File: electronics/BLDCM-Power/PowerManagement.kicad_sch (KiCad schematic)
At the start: 4 parts, among them U2 LDL212PV33R, U7 TPS2120

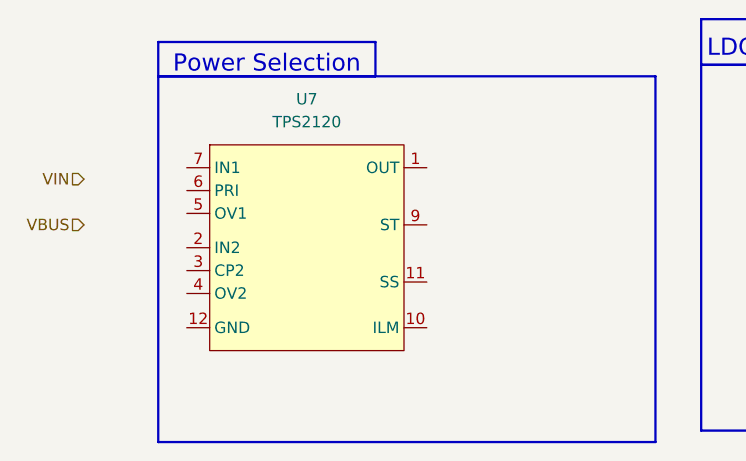
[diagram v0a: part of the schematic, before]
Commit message: Fix(pcb): Add missing USB CC1 pull-down
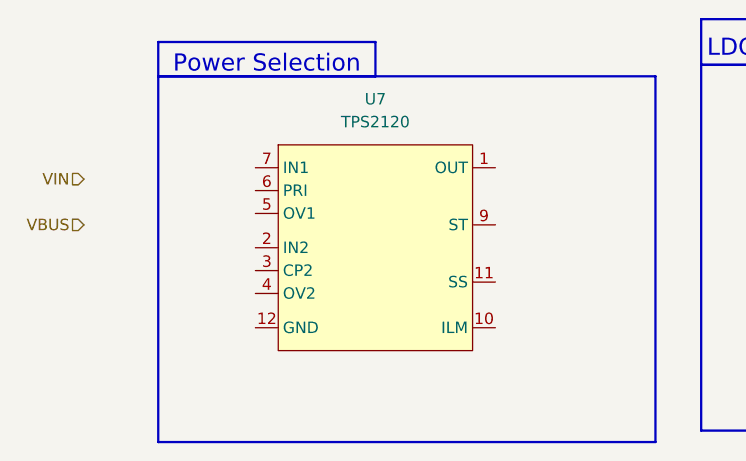
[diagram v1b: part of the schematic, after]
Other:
- moved on the sheet: U7
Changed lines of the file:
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@@
 	(symbol
 		(lib_id "BrenoCQ:TPS2120")
-		(at 63.5 53.34 0)
+		(at 71.12 53.34 0)
 		(unit 1)
 		(exclude_from_sim no)
@@
 		(fields_autoplaced yes)
 		(property "Reference" "U7"
-			(at 62.865 31.75 0)
+			(at 70.485 31.75 0)
 			(effects
 				(font
@@
 		)
 		(property "Value" "TPS2120"
-			(at 62.865 34.29 0)
+			(at 70.485 34.29 0)
 			(effects
 				(font
@@
 		)
 		(property "Footprint" ""
-			(at 63.5 53.34 0)
+			(at 71.12 53.34 0)
 			(effects
 				(font
@@
 		)
 		(property "Datasheet" "https://www.ti.com/lit/ds/symlink/tps2120.pdf?ts=1748897252786&ref_url=https%253A%252F%252Fwww.ti.com%252Fproduct%252FTPS2120"
-			(at 63.5 64.77 0)
+			(at 71.12 64.77 0)
 			(effects
 				(font
@@
 		)
 		(property "Description" "TPS2120 2.8-V to 22-V Priority Power MUX with Seamless Switchover"
-			(at 63.5 62.23 0)
+			(at 71.12 62.23 0)
 			(effects
 				(font

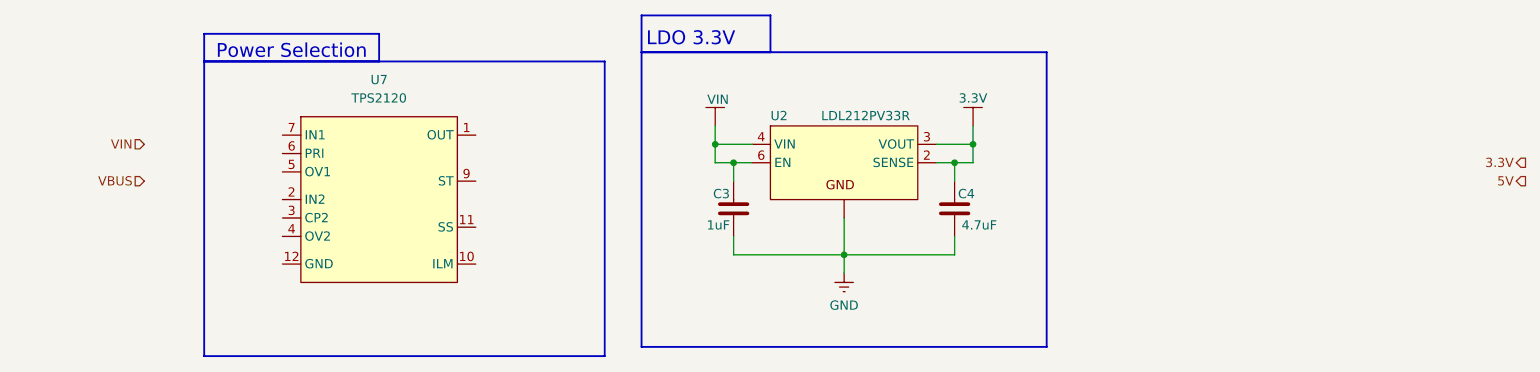
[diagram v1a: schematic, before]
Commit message: Feat(schematic): Automatic power source selection
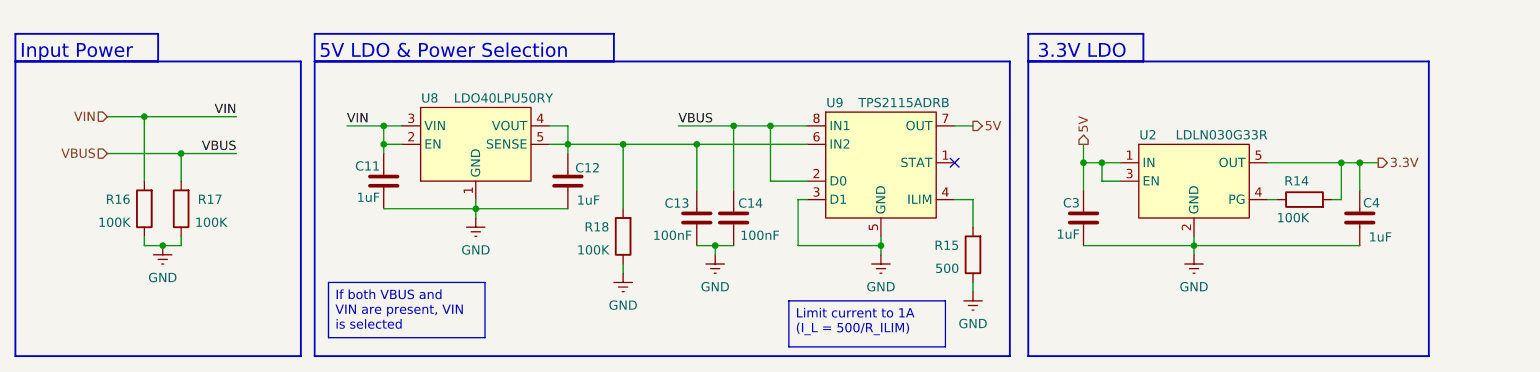
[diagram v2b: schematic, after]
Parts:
- removed U2: LDL212PV33R, BrenoCQ:DFN-6-2x2, symbol BrenoCQ:LDL212PV33R
- removed U7: TPS2120, symbol BrenoCQ:TPS2120
- added C11, C12: 1uF, BrenoCQ:C_0402, symbol BrenoCQ:C
- added C13, C14: 100nF, BrenoCQ:C_0402, symbol BrenoCQ:C
- added R14, R16, R17, R18: 100K, BrenoCQ:R_0402, symbol Device:R
- added R15: 500, BrenoCQ:R_0402, symbol Device:R
- added U2: LDLN030G33R, BrenoCQ:TSOT-23-5, symbol BrenoCQ:LDLN030G33R
- added U8: LDO40LPU50RY, BrenoCQ:DFN-6-3x3, symbol BrenoCQ:LDO40LPU50RY
- added U9: TPS2115ADRB, BrenoCQ:VSON-8, symbol BrenoCQ:TPS2115ADRB
- C4: value 4.7uF -> 1uF
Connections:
- net 3.3V: now also R14.2, U2.5 (OUT)
- net 5V: now also C3.2, U2.1 (IN), U2.3 (EN), U9.7 (OUT)
- net GND: now also C11.1, C12.1, C13.2, C14.2, R15.1, R16.1, R17.1, R18.1, U2.2 (GND), U8.1 (GND), U8.TAB, U9.3 (D1), U9.5 (GND), U9.PAD
- net VBUS: now also C14.1, R17.2, U9.2 (D0), U9.8 (IN1)
- net VIN: now also C11.2, R16.2, U8.2 (EN), U8.3 (VIN); no longer C3.2
- new net: R15.2, U9.4 (ILIM)
- new net: C12.2, C13.1, R18.2, U8.4 (VOUT), U8.5 (SENSE), U9.6 (IN2)
- new net: R14.1, U2.4 (PG)
- no-connect marks 0 -> 1
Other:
- note added: "3.3V LDO"
- note added: "5V LDO & Power Selection"
- note added: "Input Power"
- note removed: "LDO 3.3V"
- note removed: "Power Selection"
- moved on the sheet: C3, C4

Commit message: Feat(schematic): Update volt sense to use BAT54S
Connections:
- net GND: now also U8.PAD; no longer U8.TAB
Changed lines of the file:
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@@
 		(pin "6"
 		)
-		(pin "TAB"
+		(pin "PAD"
 		)
 		(pin "4"

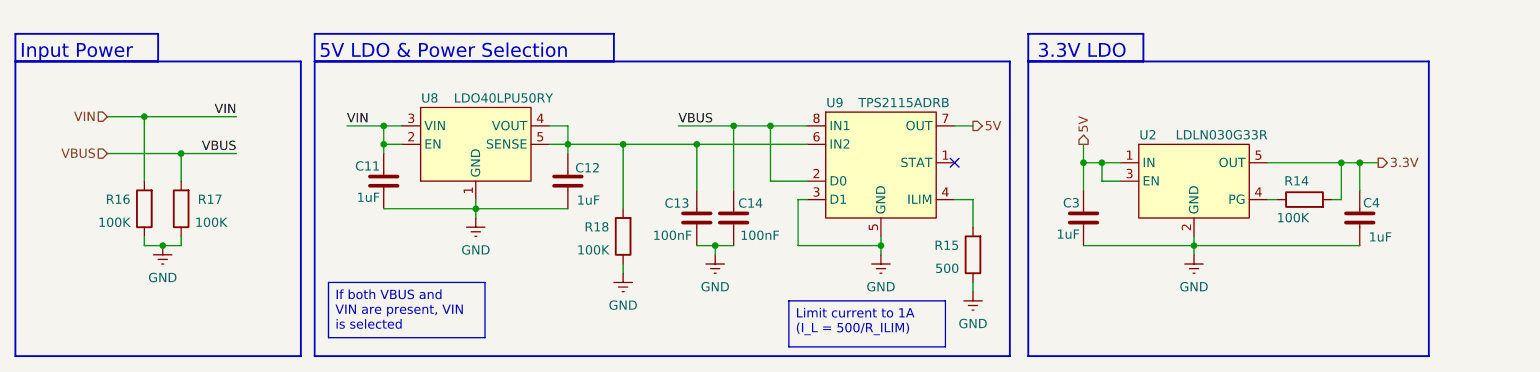
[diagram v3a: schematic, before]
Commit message: Feat(schematic): Replace current sense resistors
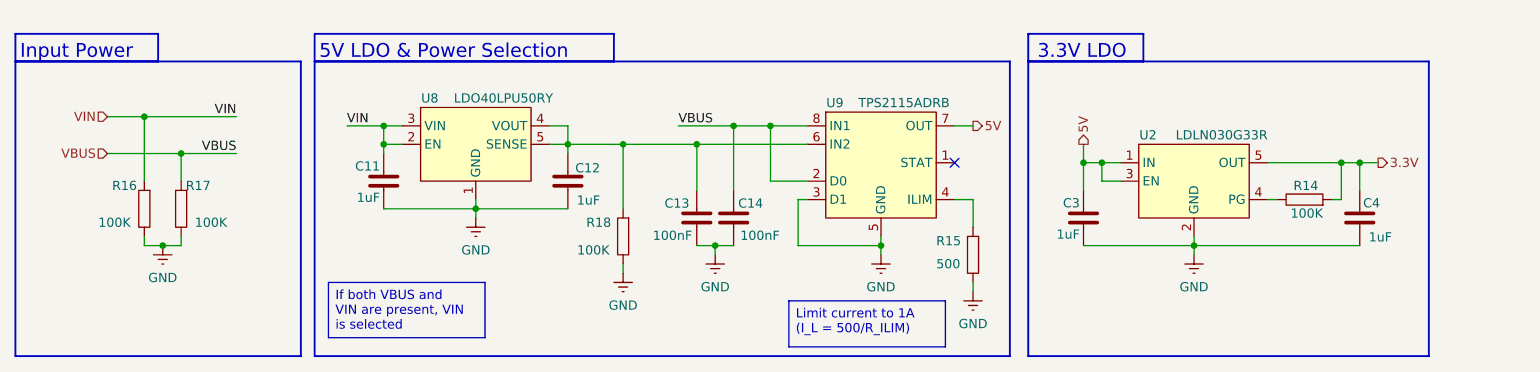
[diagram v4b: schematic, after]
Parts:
- R14, R15, R16, R17, R18: symbol Device:R -> BrenoCQ:R
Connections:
- net 3.3V: now also R14.1; no longer R14.2
- net GND: now also R15.2, R16.2, R17.2, R18.2; no longer R15.1, R16.1, R17.1, R18.1
- net VBUS: now also R17.1; no longer R17.2
- net VIN: now also R16.1; no longer R16.2
- net at U9.4 (ILIM): now also R15.1; no longer R15.2
- net at C12.2, C13.1, U8.4 (VOUT)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: now also R18.1; no longer R18.2
- net at U2.4 (PG): now also R14.2; no longer R14.1
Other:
- moved on the sheet: R14, R15, R16, R17, R18
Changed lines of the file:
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@@
 	)
 	(symbol
-		(lib_id "Device:R")
-		(at 43.18 49.53 180)
+		(lib_id "BrenoCQ:R")
+		(at 43.18 49.53 270)
 		(unit 1)
 		(exclude_from_sim no)
@@
 		(dnp no)
 		(property "Reference" "R17"
-			(at 48.895 48.26 0)
+			(at 43.815 46.355 90)
 			(effects
 				(font
@@
 		)
 		(property "Value" "100K"
-			(at 45.085 51.435 0)
+			(at 49.53 51.435 90)
 			(effects
 				(font
@@
 		)
 		(property "Footprint" "BrenoCQ:R_0402"
-			(at 44.958 49.53 90)
+			(at 43.18 47.752 90)
 			(effects
 				(font
@@
 		)
 		(property "Description" "Resistor"
-			(at 43.18 49.53 0)
+			(at 41.275 49.53 0)
 			(effects
 				(font
@@
 	)
 	(symbol
-		(lib_id "Device:R")
-		(at 38.1 49.53 180)
+		(lib_id "BrenoCQ:R")
+		(at 38.1 49.53 270)
 		(unit 1)
 		(exclude_from_sim no)
@@
 		(dnp no)
 		(property "Reference" "R16"
-			(at 36.195 48.26 0)
+			(at 33.655 46.355 90)
 			(effects
 				(font
@@
 		)
 		(property "Value" "100K"
-			(at 36.195 51.435 0)
+			(at 31.75 51.435 90)
 			(effects
 				(font
@@
 		)
 		(property "Footprint" "BrenoCQ:R_0402"
-			(at 39.878 49.53 90)
+			(at 38.1 47.752 90)
 			(effects
 				(font
@@
 		)
 		(property "Description" "Resistor"
-			(at 38.1 49.53 0)
+			(at 36.195 49.53 0)
 			(effects
 				(font
@@
 	)
 	(symbol
-		(lib_id "Device:R")
-		(at 152.4 55.88 180)
+		(lib_id "BrenoCQ:R")
+		(at 152.4 55.88 270)
 		(unit 1)
 		(exclude_from_sim no)
@@
 		(dnp no)
 		(property "Reference" "R15"
-			(at 150.495 54.61 0)
+			(at 147.32 53.975 90)
 			(effects
 				(font
@@
 		)
 		(property "Value" "500"
-			(at 150.495 57.785 0)
+			(at 147.32 57.15 90)
 			(effects
 				(font
@@
 		)
 		(property "Footprint" "BrenoCQ:R_0402"
-			(at 154.178 55.88 90)
+			(at 152.4 54.102 90)
 			(effects
 				(font
@@
 		)
 		(property "Description" "Resistor"
-			(at 152.4 55.88 0)
+			(at 150.495 55.88 0)
 			(effects
 				(font
@@
 	)
 	(symbol
-		(lib_id "Device:R")
-		(at 104.14 53.34 180)
+		(lib_id "BrenoCQ:R")
+		(at 104.14 53.34 270)
 		(unit 1)
 		(exclude_from_sim no)
@@
 		(dnp no)
 		(property "Reference" "R18"
-			(at 102.235 52.07 0)
+			(at 99.06 51.435 90)
 			(effects
 				(font
@@
 		)
 		(property "Value" "100K"
-			(at 102.235 55.245 0)
+			(at 97.79 55.245 90)
 			(effects
 				(font
@@
 		)
 		(property "Footprint" "BrenoCQ:R_0402"
-			(at 105.918 53.34 90)
+			(at 104.14 51.562 90)
 			(effects
 				(font
@@
 		)
 		(property "Description" "Resistor"
-			(at 104.14 53.34 0)
+			(at 102.235 53.34 0)
 			(effects
 				(font
@@
 	)
 	(symbol
-		(lib_id "Device:R")
-		(at 198.12 48.26 90)
+		(lib_id "BrenoCQ:R")
+		(at 198.12 48.26 180)
 		(unit 1)
 		(exclude_from_sim no)
@@
 		(dnp no)
 		(property "Reference" "R14"
-			(at 198.755 45.72 90)
+			(at 200.025 46.355 0)
 			(effects
 				(font
@@
 		)
 		(property "Value" "100K"
-			(at 198.755 50.8 90)
+			(at 200.66 50.165 0)
 			(effects
 				(font
@@
 		)
 		(property "Footprint" "BrenoCQ:R_0402"
-			(at 198.12 50.038 90)
+			(at 199.898 48.26 90)
 			(effects
 				(font
@@
 		)
 		(property "Description" "Resistor"
-			(at 198.12 48.26 0)
-			(effects
-				(font
+			(at 198.12 46.355 0)
+			(effects
+				(font

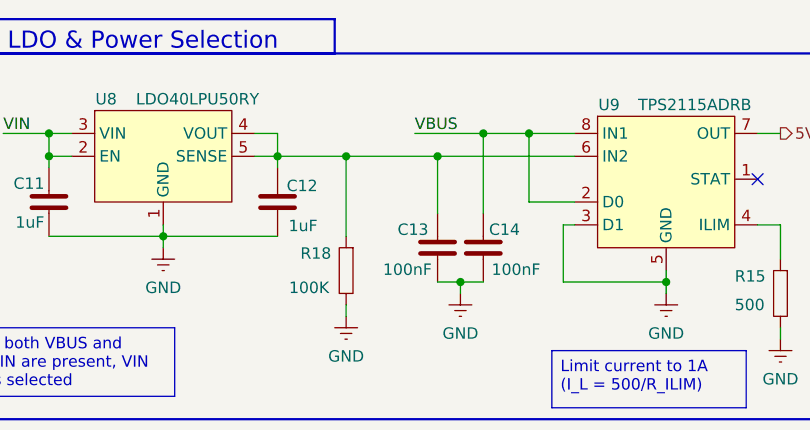
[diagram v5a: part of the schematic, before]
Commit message: Feat(pcb): Route power management
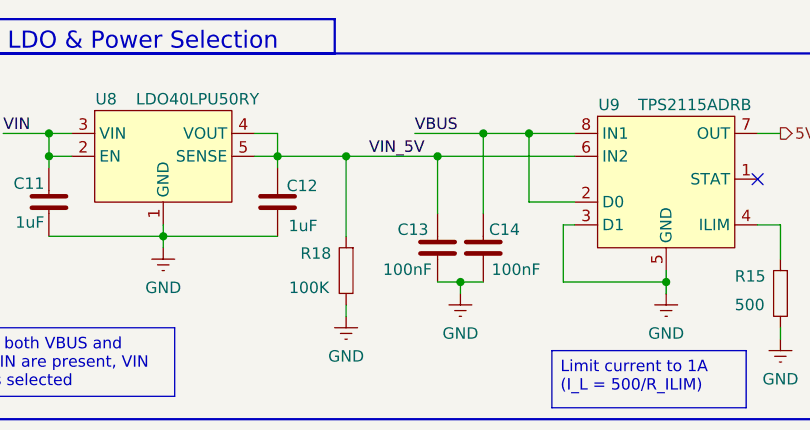
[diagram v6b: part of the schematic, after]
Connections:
- net VIN_5V: now reaches C12.2, C13.1, R18.1, U8.4 (VOUT), U8.5 (SENSE), U9.6 (IN2)
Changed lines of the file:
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@@
+		)
+	)
+	(label "VIN_5V"
+		(at 106.68 40.64 0)
+		(effects
+			(font
+				(size 1.27 1.27)
+			)
+			(justify left bottom)
 		)
 	)

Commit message: Feat: Add schematic PDFs for v1.0 PCBs
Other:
- company: (none) -> Breno Cunha Queiroz
- title: (none) -> BLDCM Power - Power Management
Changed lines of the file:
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@@
 	(generator_version "9.0")
 	(paper "A4")
+	(title_block
+		(title "BLDCM Power - Power Management")
+		(date "2025-07-19")
+		(rev "v1.0")
+		(company "Breno Cunha Queiroz")
+	)
 	(rectangle
 		(start 20.32 25.4)
